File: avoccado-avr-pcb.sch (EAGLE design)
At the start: 30 parts, among them IC1 MCP1703CB, IC5 ATMEGA328P-20MU, Q1 #MHz, Q2 MOSFET-NCHANNEL2N7002PW, U1 ATMEGA328P, U2 MCP73831, X1 Micro USB

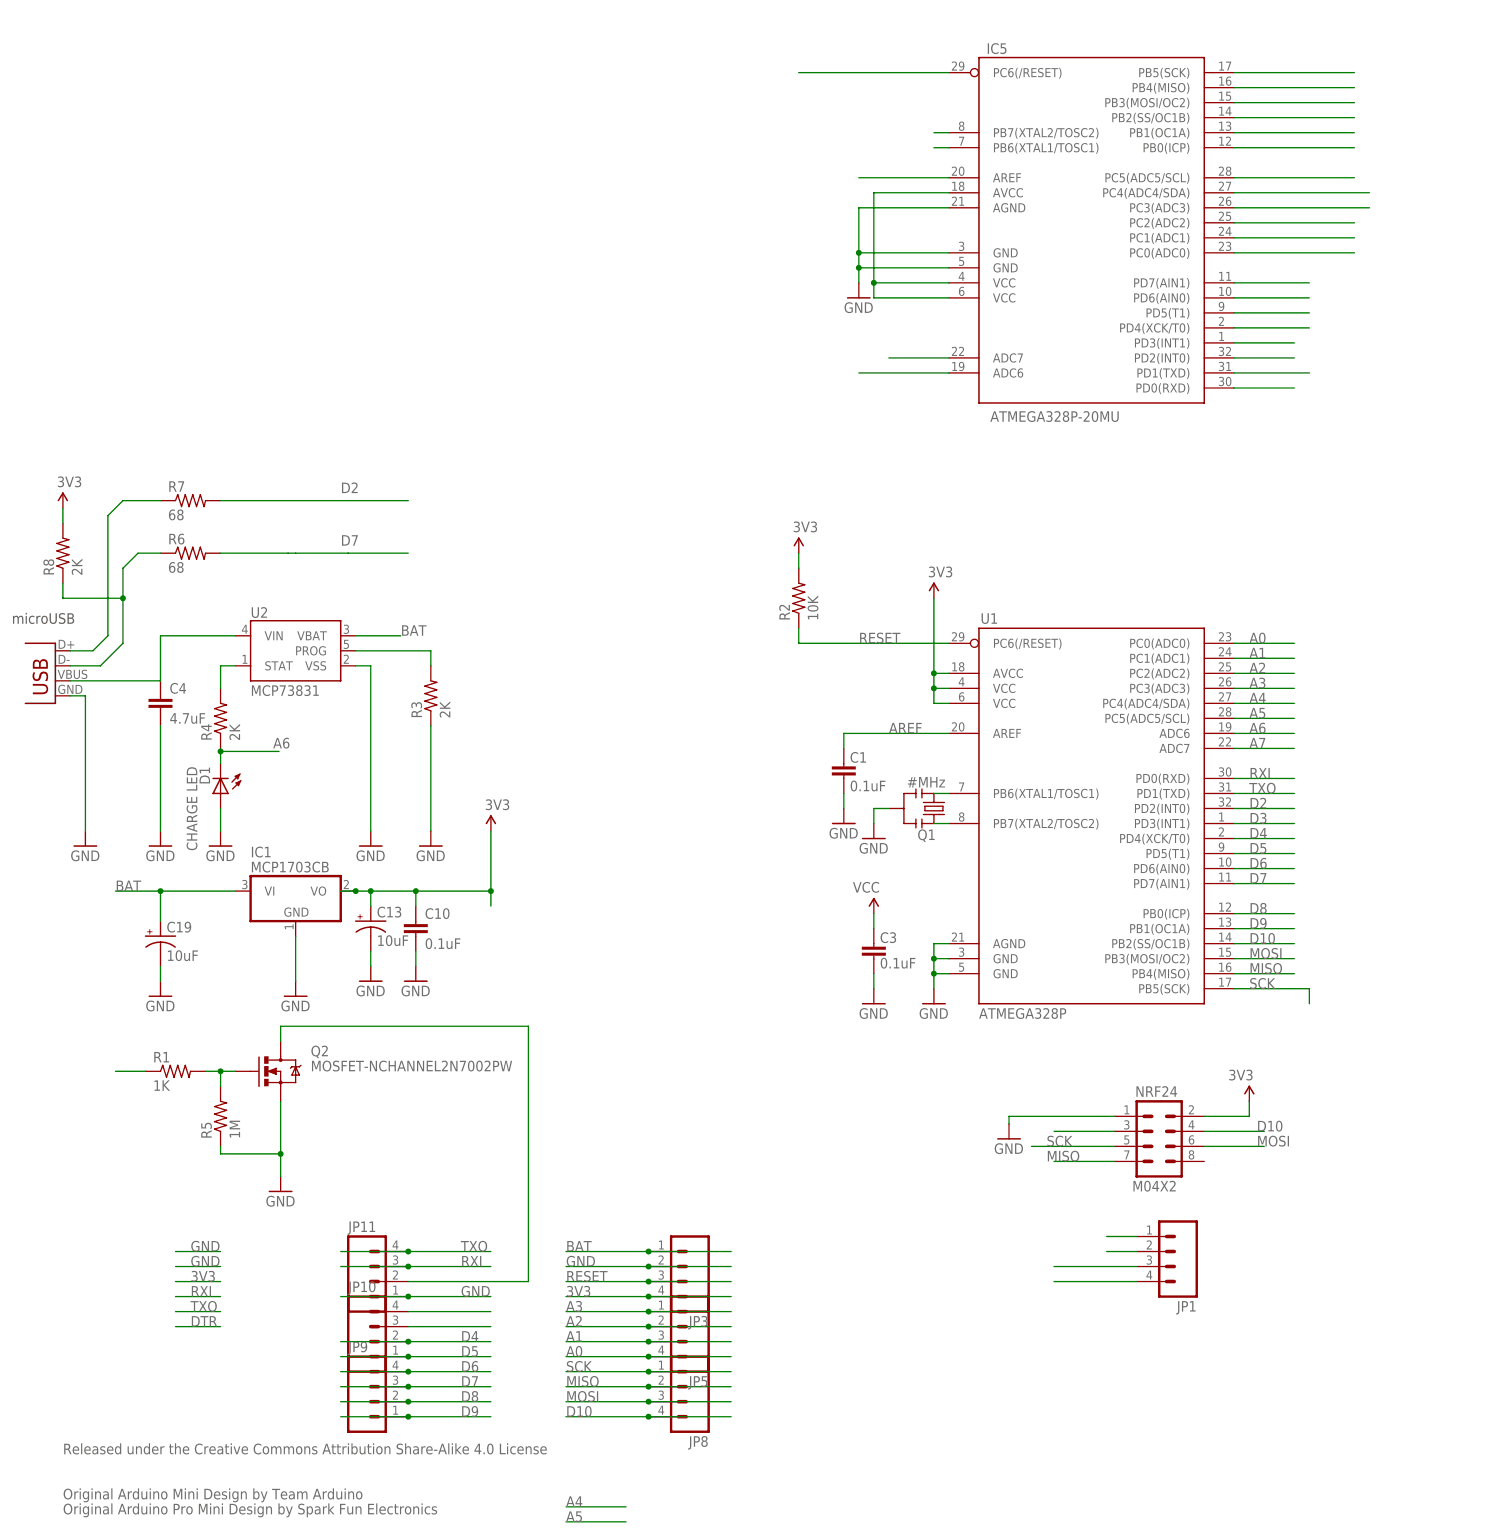
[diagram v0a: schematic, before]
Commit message: corrected DRC errors, mostly spacing
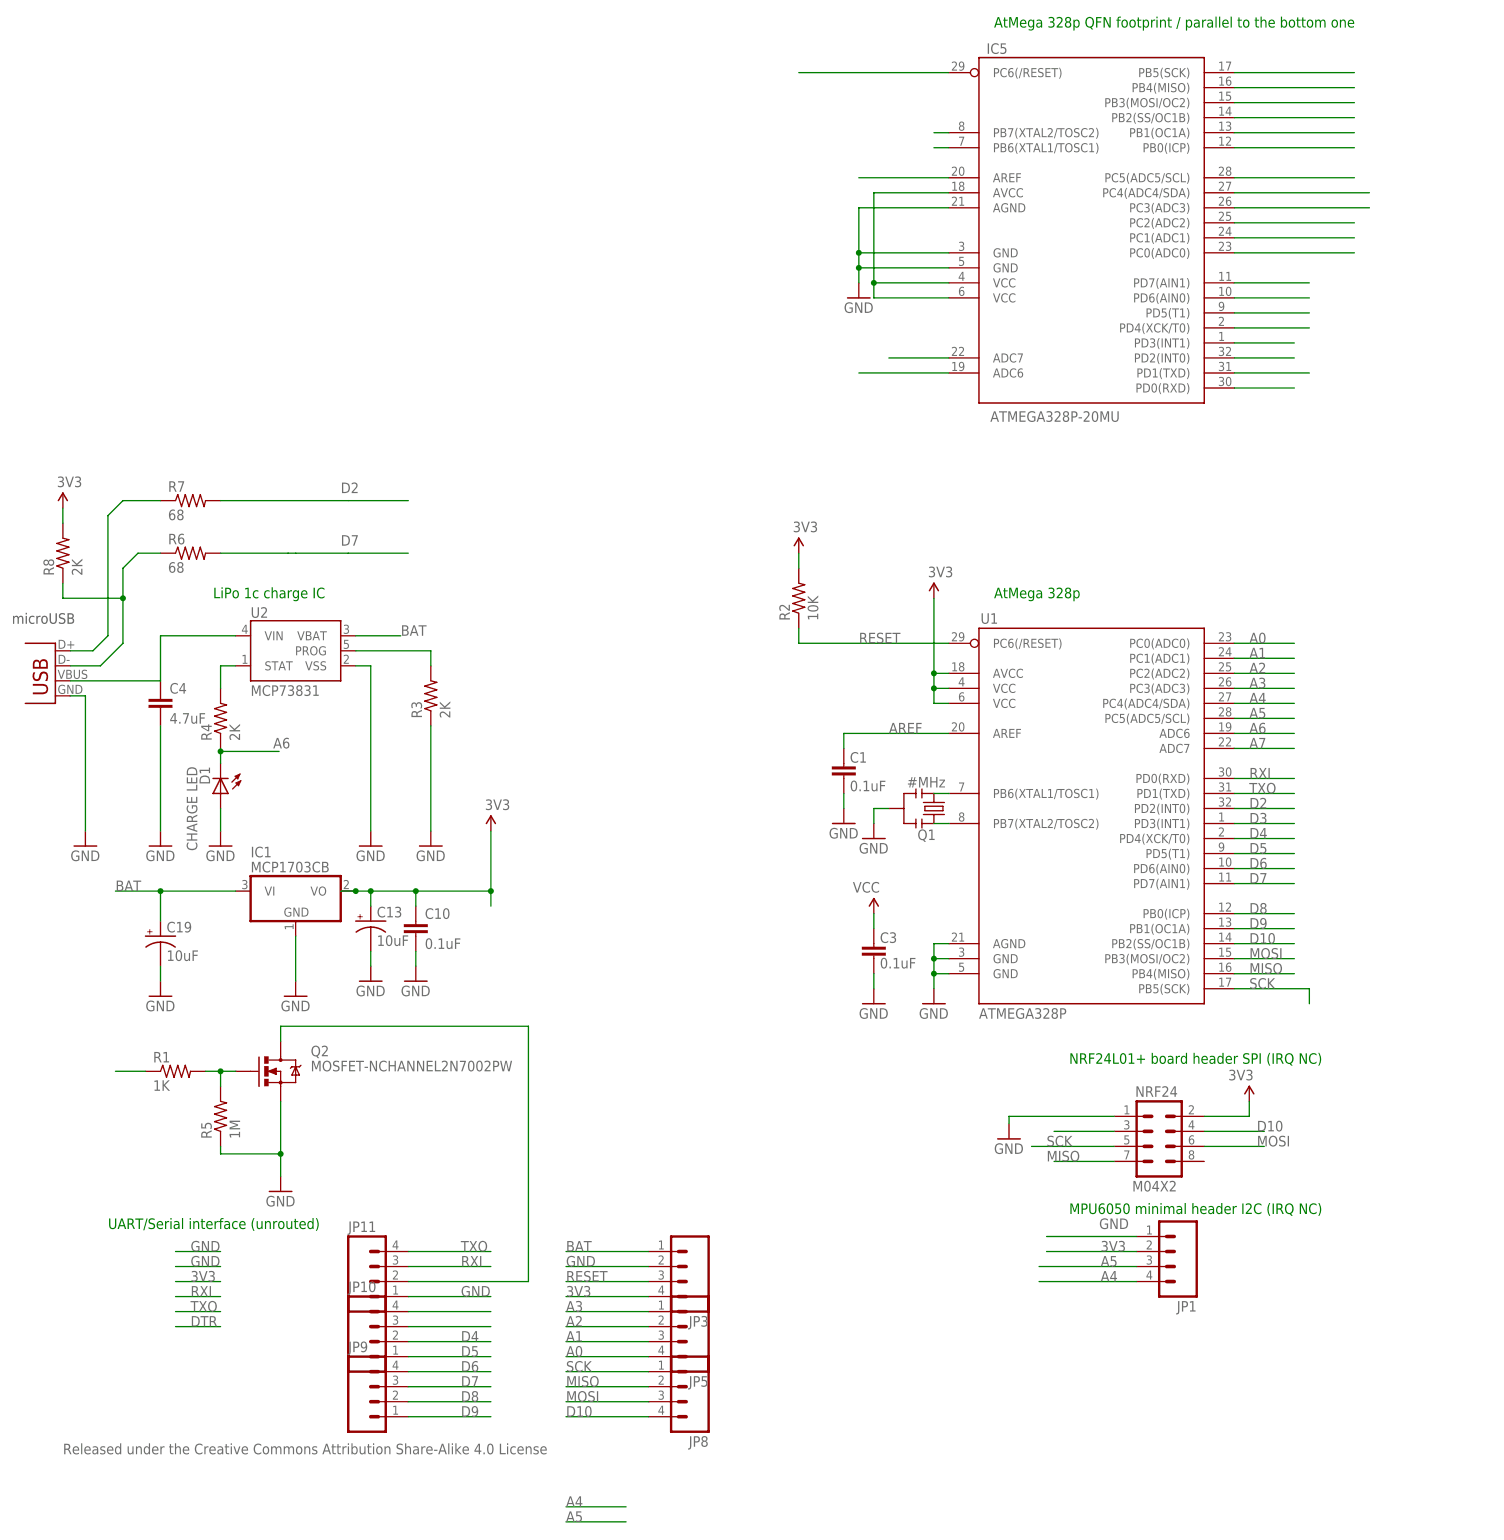
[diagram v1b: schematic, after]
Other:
- note added: "AtMega 328p"
- note added: "AtMega 328p QFN footprint / parallel to the bottom one"
- note added: "LiPo 1c charge IC"
- note added: "MPU6050 minimal header I2C (IRQ NC)"
- note added: "NRF24L01+ board header SPI (IRQ NC)"
- note added: "UART/Serial interface (unrouted)"
- note removed: "Original Arduino Mini Design by Team Arduino"
- note removed: "Original Arduino Pro Mini Design by Spark Fun Electronics"
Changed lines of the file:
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@@
 <plain>
 <text x="17.78" y="17.78" size="1.778" layer="95">Released under the Creative Commons Attribution Share-Alike 4.0 License</text>
-<text x="17.78" y="10.16" size="1.778" layer="95">Original Arduino Mini Design by Team Arduino</text>
-<text x="17.78" y="7.62" size="1.778" layer="95">Original Arduino Pro Mini Design by Spark Fun Electronics</text>
 <text x="9.144" y="158.242" size="1.778" layer="97">microUSB</text>
+<text x="187.96" y="83.82" size="1.778" layer="91">NRF24L01+ board header SPI (IRQ NC)</text>
+<text x="187.96" y="58.42" size="1.778" layer="91">MPU6050 minimal header I2C (IRQ NC)</text>
+<text x="175.26" y="162.56" size="1.778" layer="91">AtMega 328p</text>
+<text x="175.26" y="259.08" size="1.778" layer="91">AtMega 328p QFN footprint / parallel to the bottom one</text>
+<text x="43.18" y="162.56" size="1.778" layer="91">LiPo 1c charge IC</text>
+<text x="25.4" y="55.88" size="1.778" layer="91">UART/Serial interface (unrouted)</text>
 </plain>
 <instances>
@@
 <segment>
 <label x="85.09" y="44.45" size="1.778" layer="95"/>
-<wire x1="64.77" y1="44.45" x2="76.2" y2="44.45" width="0.1524" layer="91"/>
 <pinref part="JP11" gate="G$1" pin="1"/>
 <wire x1="76.2" y1="44.45" x2="90.17" y2="44.45" width="0.1524" layer="91"/>
-<junction x="76.2" y="44.45"/>
 </segment>
 <segment>
 <label x="102.87" y="49.53" size="1.778" layer="95"/>
-<wire x1="130.81" y1="49.53" x2="116.84" y2="49.53" width="0.1524" layer="91"/>
 <pinref part="JP3" gate="G$1" pin="2"/>
 <wire x1="116.84" y1="49.53" x2="102.87" y2="49.53" width="0.1524" layer="91"/>
-<junction x="116.84" y="49.53"/>
 </segment>
 <segment>
@@
 </segment>
 <segment>
-<wire x1="199.39" y1="54.61" x2="194.31" y2="54.61" width="0.1524" layer="91"/>
+<wire x1="199.39" y1="54.61" x2="184.15" y2="54.61" width="0.1524" layer="91"/>
 <pinref part="JP1" gate="G$1" pin="1"/>
+<label x="193.04" y="55.88" size="1.778" layer="95"/>
 </segment>
 <segment>
@@
 <segment>
 <label x="102.87" y="46.99" size="1.778" layer="95"/>
-<wire x1="130.81" y1="46.99" x2="116.84" y2="46.99" width="0.1524" layer="91"/>
 <pinref part="JP3" gate="G$1" pin="3"/>
 <wire x1="116.84" y1="46.99" x2="102.87" y2="46.99" width="0.1524" layer="91"/>
-<junction x="116.84" y="46.99"/>
 </segment>
 <segment>
@@
 <segment>
 <label x="102.87" y="31.75" size="1.778" layer="95"/>
-<wire x1="130.81" y1="31.75" x2="116.84" y2="31.75" width="0.1524" layer="91"/>
 <pinref part="JP8" gate="G$1" pin="1"/>
 <wire x1="116.84" y1="31.75" x2="102.87" y2="31.75" width="0.1524" layer="91"/>
-<junction x="116.84" y="31.75"/>
 </segment>
 <segment>
@@
 <segment>
 <label x="102.87" y="29.21" size="1.778" layer="95"/>
-<wire x1="130.81" y1="29.21" x2="116.84" y2="29.21" width="0.1524" layer="91"/>
 <pinref part="JP8" gate="G$1" pin="2"/>
 <wire x1="116.84" y1="29.21" x2="102.87" y2="29.21" width="0.1524" layer="91"/>
-<junction x="116.84" y="29.21"/>
 </segment>
 <segment>
@@
 <segment>
 <label x="102.87" y="26.67" size="1.778" layer="95"/>
-<wire x1="130.81" y1="26.67" x2="116.84" y2="26.67" width="0.1524" layer="91"/>
 <pinref part="JP8" gate="G$1" pin="3"/>
 <wire x1="116.84" y1="26.67" x2="102.87" y2="26.67" width="0.1524" layer="91"/>
-<junction x="116.84" y="26.67"/>
 </segment>
 <segment>
@@
 <segment>
 <label x="85.09" y="52.07" size="1.778" layer="95"/>
-<wire x1="64.77" y1="52.07" x2="76.2" y2="52.07" width="0.1524" layer="91"/>
 <pinref part="JP11" gate="G$1" pin="4"/>
 <wire x1="76.2" y1="52.07" x2="90.17" y2="52.07" width="0.1524" layer="91"/>
-<junction x="76.2" y="52.07"/>
 </segment>
 <segment>
@@
 <segment>
 <label x="102.87" y="44.45" size="1.778" layer="95"/>
-<wire x1="130.81" y1="44.45" x2="116.84" y2="44.45" width="0.1524" layer="91"/>
 <pinref part="JP3" gate="G$1" pin="4"/>
 <wire x1="116.84" y1="44.45" x2="102.87" y2="44.45" width="0.1524" layer="91"/>
-<junction x="116.84" y="44.45"/>
 </segment>
 <segment>
@@
 </segment>
 <segment>
-<wire x1="199.39" y1="52.07" x2="194.31" y2="52.07" width="0.1524" layer="91"/>
+<wire x1="199.39" y1="52.07" x2="184.15" y2="52.07" width="0.1524" layer="91"/>
 <pinref part="JP1" gate="G$1" pin="2"/>
+<label x="193.294" y="52.07" size="1.778" layer="95"/>
 </segment>
 <segment>
@@
 <segment>
 <label x="85.09" y="24.13" size="1.778" layer="95"/>
-<wire x1="64.77" y1="24.13" x2="76.2" y2="24.13" width="0.1524" layer="91"/>
 <pinref part="JP9" gate="G$1" pin="1"/>
 <wire x1="76.2" y1="24.13" x2="90.17" y2="24.13" width="0.1524" layer="91"/>
-<junction x="76.2" y="24.13"/>
 </segment>
 <segment>
@@
 <wire x1="90.17" y1="26.67" x2="76.2" y2="26.67" width="0.1524" layer="91"/>
 <pinref part="JP9" gate="G$1" pin="2"/>
-<wire x1="76.2" y1="26.67" x2="64.77" y2="26.67" width="0.1524" layer="91"/>
-<junction x="76.2" y="26.67"/>
 </segment>
 <segment>
@@
 </segment>
 <segment>
-<wire x1="185.42" y1="49.53" x2="199.39" y2="49.53" width="0.1524" layer="91"/>
+<wire x1="182.88" y1="49.53" x2="199.39" y2="49.53" width="0.1524" layer="91"/>
 <pinref part="JP1" gate="G$1" pin="3"/>
+<label x="193.294" y="49.53" size="1.778" layer="95"/>
 </segment>
 <segment>
@@
 </segment>
 <segment>
-<wire x1="185.42" y1="46.99" x2="199.39" y2="46.99" width="0.1524" layer="91"/>
+<wire x1="182.88" y1="46.99" x2="199.39" y2="46.99" width="0.1524" layer="91"/>
 <pinref part="JP1" gate="G$1" pin="4"/>
+<label x="193.294" y="46.99" size="1.778" layer="95"/>
 </segment>
 <segment>
@@
 <segment>
 <label x="102.87" y="41.91" size="1.778" layer="95"/>
-<wire x1="130.81" y1="41.91" x2="116.84" y2="41.91" width="0.1524" layer="91"/>
 <pinref part="JP5" gate="G$1" pin="1"/>
 <wire x1="116.84" y1="41.91" x2="102.87" y2="41.91" width="0.1524" layer="91"/>
-<junction x="116.84" y="41.91"/>
 </segment>
 <segment>
@@
 <segment>
 <label x="102.87" y="39.37" size="1.778" layer="95"/>
-<wire x1="130.81" y1="39.37" x2="116.84" y2="39.37" width="0.1524" layer="91"/>
 <pinref part="JP5" gate="G$1" pin="2"/>
 <wire x1="116.84" y1="39.37" x2="102.87" y2="39.37" width="0.1524" layer="91"/>
-<junction x="116.84" y="39.37"/>
 </segment>
 <segment>
@@
 <segment>
 <label x="102.87" y="36.83" size="1.778" layer="95"/>
-<wire x1="130.81" y1="36.83" x2="116.84" y2="36.83" width="0.1524" layer="91"/>
 <pinref part="JP5" gate="G$1" pin="3"/>
 <wire x1="116.84" y1="36.83" x2="102.87" y2="36.83" width="0.1524" layer="91"/>
-<junction x="116.84" y="36.83"/>
 </segment>
 <segment>
@@
 <segment>
 <label x="102.87" y="34.29" size="1.778" layer="95"/>
-<wire x1="130.81" y1="34.29" x2="116.84" y2="34.29" width="0.1524" layer="91"/>
 <pinref part="JP5" gate="G$1" pin="4"/>
 <wire x1="116.84" y1="34.29" x2="102.87" y2="34.29" width="0.1524" layer="91"/>
-<junction x="116.84" y="34.29"/>
 </segment>
 <segment>
@@
 <wire x1="90.17" y1="36.83" x2="76.2" y2="36.83" width="0.1524" layer="91"/>
 <pinref part="JP10" gate="G$1" pin="2"/>
-<wire x1="76.2" y1="36.83" x2="64.77" y2="36.83" width="0.1524" layer="91"/>
-<junction x="76.2" y="36.83"/>
 </segment>
 <segment>
@@
 <segment>
 <label x="85.09" y="34.29" size="1.778" layer="95"/>
-<wire x1="64.77" y1="34.29" x2="76.2" y2="34.29" width="0.1524" layer="91"/>
 <pinref part="JP10" gate="G$1" pin="1"/>
 <wire x1="76.2" y1="34.29" x2="90.17" y2="34.29" width="0.1524" layer="91"/>
-<junction x="76.2" y="34.29"/>
 </segment>
 <segment>
@@
 <segment>
 <label x="85.09" y="31.75" size="1.778" layer="95"/>
-<wire x1="64.77" y1="31.75" x2="76.2" y2="31.75" width="0.1524" layer="91"/>
 <pinref part="JP9" gate="G$1" pin="4"/>
 <wire x1="76.2" y1="31.75" x2="90.17" y2="31.75" width="0.1524" layer="91"/>
-<junction x="76.2" y="31.75"/>
 </segment>
 <segment>
@@
 <segment>
 <label x="85.09" y="29.21" size="1.778" layer="95"/>
-<wire x1="64.77" y1="29.21" x2="76.2" y2="29.21" width="0.1524" layer="91"/>
 <pinref part="JP9" gate="G$1" pin="3"/>
 <wire x1="76.2" y1="29.21" x2="90.17" y2="29.21" width="0.1524" layer="91"/>
-<junction x="76.2" y="29.21"/>
 </segment>
 <segment>
@@
 <segment>
 <label x="102.87" y="24.13" size="1.778" layer="95"/>
-<wire x1="130.81" y1="24.13" x2="116.84" y2="24.13" width="0.1524" layer="91"/>
 <pinref part="JP8" gate="G$1" pin="4"/>
 <wire x1="116.84" y1="24.13" x2="102.87" y2="24.13" width="0.1524" layer="91"/>
-<junction x="116.84" y="24.13"/>
 </segment>
 <segment>
@@
 <segment>
 <label x="85.09" y="49.53" size="1.778" layer="95"/>
-<wire x1="64.77" y1="49.53" x2="76.2" y2="49.53" width="0.1524" layer="91"/>
 <pinref part="JP11" gate="G$1" pin="3"/>
 <wire x1="76.2" y1="49.53" x2="90.17" y2="49.53" width="0.1524" layer="91"/>
-<junction x="76.2" y="49.53"/>
 </segment>
 <segment>
@@
 <segment>
 <label x="102.87" y="52.07" size="1.778" layer="95"/>
-<wire x1="130.81" y1="52.07" x2="116.84" y2="52.07" width="0.1524" layer="91"/>
 <pinref part="JP3" gate="G$1" pin="1"/>
 <wire x1="116.84" y1="52.07" x2="102.87" y2="52.07" width="0.1524" layer="91"/>
-<junction x="116.84" y="52.07"/>
-</segment>
-</net>
+</segment>
+</net>
